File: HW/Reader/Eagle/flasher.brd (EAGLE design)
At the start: 100 x 80 mm, 26 parts, among them Q1 12Mhz, Q1A MMBT3904, Q1B MMBT3904, X1 MINI-USB-SCHIELD-32005-201

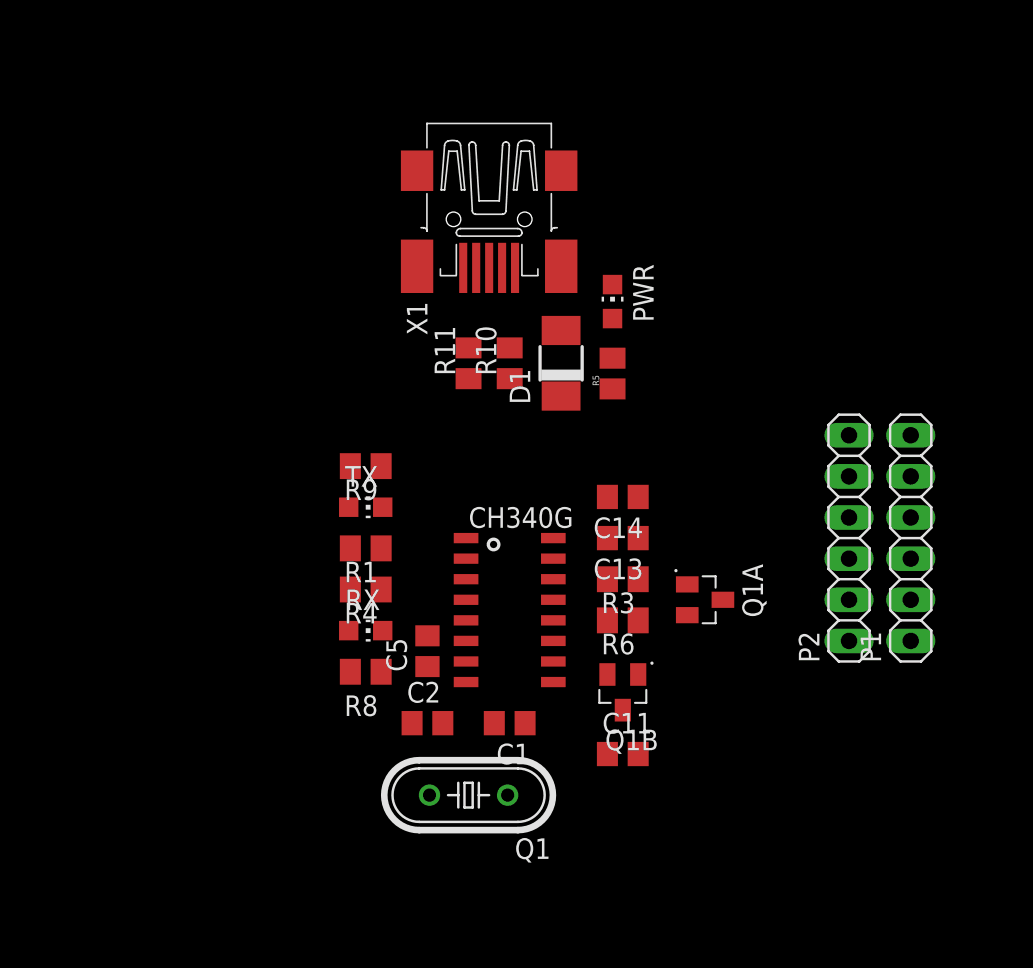
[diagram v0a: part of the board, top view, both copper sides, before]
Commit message: Flasher CH340G SCH & PCB
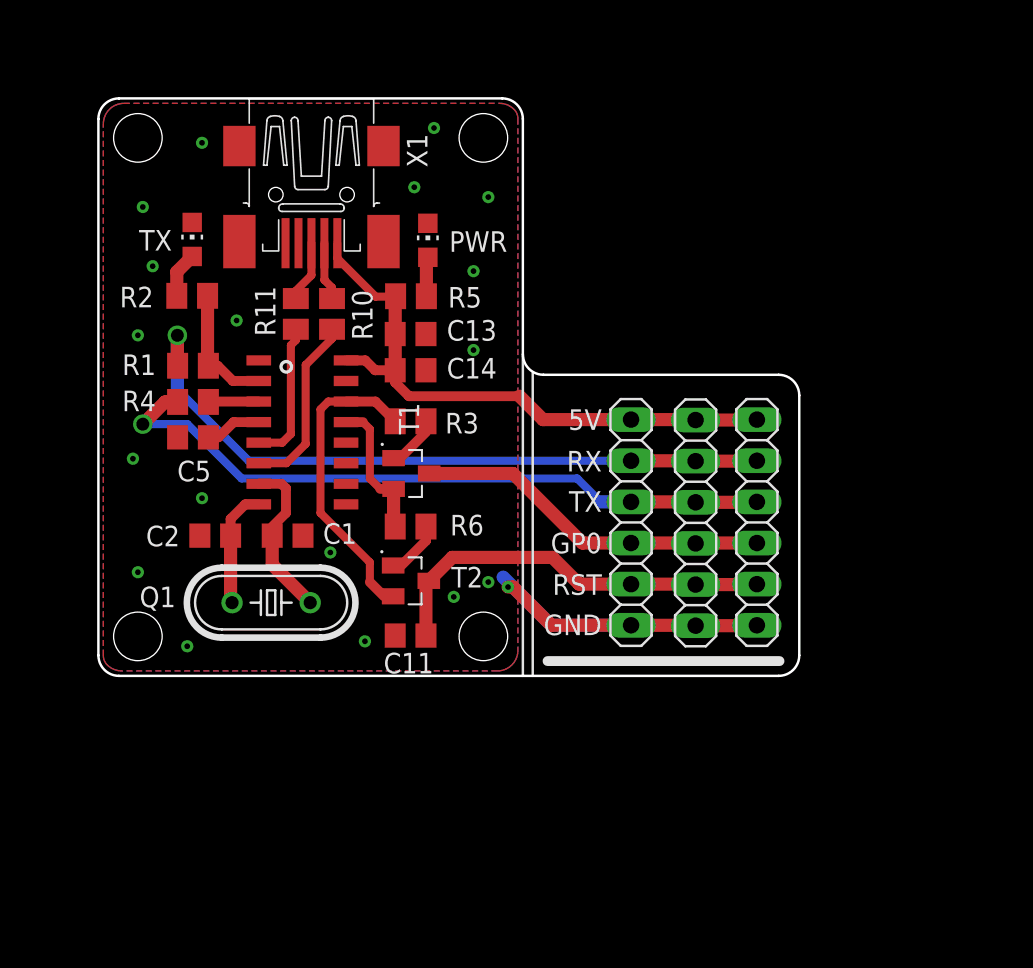
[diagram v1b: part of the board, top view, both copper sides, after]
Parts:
- removed D1: SS14, diode:DO-214AC
- removed Q1A, Q1B: MMBT3904, MMBT3904:SOT95P240X120-3N
- removed R8, R9: 470, rcl:M0805
- removed RX: (no value), led:CHIP-LED0805
- removed U$1: CH340G, ch340g:SOIC16
- added P3: (no value), pinhead:1X06
- added R2: 470, rcl:M0805
- added T1, T2: MMBT3904, MMBT3904:SOT95P240X120-3N
- added U1: CH340G, ch340g:SOIC16
- moved TX 19.7 mm to (36.3, 48.3), turned to 0 degrees
- moved C5 19.6 mm to (36.3, 36.1), turned to 0 degrees
- moved C13 18.2 mm to (49.8, 42.4)
- moved C1 18.0 mm to (42.2, 30.0)
- moved C2 17.5 mm to (37.7, 30.0)
- moved Q1 17.0 mm to (41.1, 25.9)
- moved R3 16.3 mm to (49.8, 37.1)
- moved R4 15.7 mm to (36.3, 38.3)
- moved R1 15.5 mm to (36.3, 40.5)
- moved C14 15.3 mm to (49.8, 40.2)
- moved C11 15.0 mm to (49.8, 23.8)
- moved R6 14.3 mm to (49.8, 30.6)
- moved R5 13.3 mm to (49.8, 44.8), turned to 0 degrees
- moved PWR 12.0 mm to (50.8, 48.2)
- moved R10 11.4 mm to (44.9, 43.7)
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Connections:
- removed net N$7: R9.2, TX.A
- removed net VIN: D1.A, P1.1, P2.1, X1.1
- net +5V: now also P1.1, P2.1, P3.1, U1.16, X1.1; no longer D1.C, R8.1, R9.1, U$1.16
- net D+: now also U1.5; no longer U$1.5
- net D-: now also U1.6; no longer U$1.6
- net DTR: now also T1.2, U1.13; no longer Q1A.2, U$1.13
- net GND: now also P3.6, TX.C, U1.1; no longer U$1.1
- net GPIO0: now also P3.4, T1.3; no longer Q1A.3
- net N$1: now also R2.2, U1.2; no longer TX.C, U$1.2
- net N$12: now also U1.4; no longer U$1.4
- net N$16: now also U1.7; no longer U$1.7
- net N$17: now also U1.8; no longer U$1.8
- net N$2: now also U1.3; no longer RX.C, U$1.3
- net N$4: now also R2.1, TX.A; no longer R8.2, RX.A
- net N$5: now also T1.1; no longer Q1A.1
- net N$6: now also T2.1; no longer Q1B.1
- net RESET: now also P3.5, T2.3; no longer Q1B.3
- net RTS: now also T2.2, U1.14; no longer Q1B.2, U$1.14
- net RXD: now also P3.2
- net TXD: now also P3.3
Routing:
- net RXD: track 0.00 -> 42.9 mm, vias 0 -> 1
- net TXD: track 0.00 -> 42.6 mm, vias 0 -> 1
- net +5V: track 0.00 -> 37.4 mm
- net RESET: track 0.00 -> 25.6 mm
- net GND: track 0.00 -> 25.5 mm, vias 0 -> 19
- net GPIO0: track 0.00 -> 22.0 mm
- net RTS: track 0.00 -> 19.5 mm
- net D-: track 0.00 -> 11.1 mm
- net N$16: track 0.00 -> 10.2 mm
- net DTR: track 0.00 -> 8.80 mm
- net D+: track 0.00 -> 8.80 mm
- net N$1: track 0.00 -> 7.84 mm
- net N$17: track 0.00 -> 7.32 mm
- net N$9: track 0.00 -> 3.82 mm
- net N$8: track 0.00 -> 3.61 mm
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- added copper zone on layer 1, net GND
- added copper zone on layer 16, net GND
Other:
- outline, holes or cut-outs redrawn
- board text added: "5V"
- board text added: "GND"
- board text added: "GP0"
- board text added: "RST"
- board text added: "RX"
- board text added: "TX"

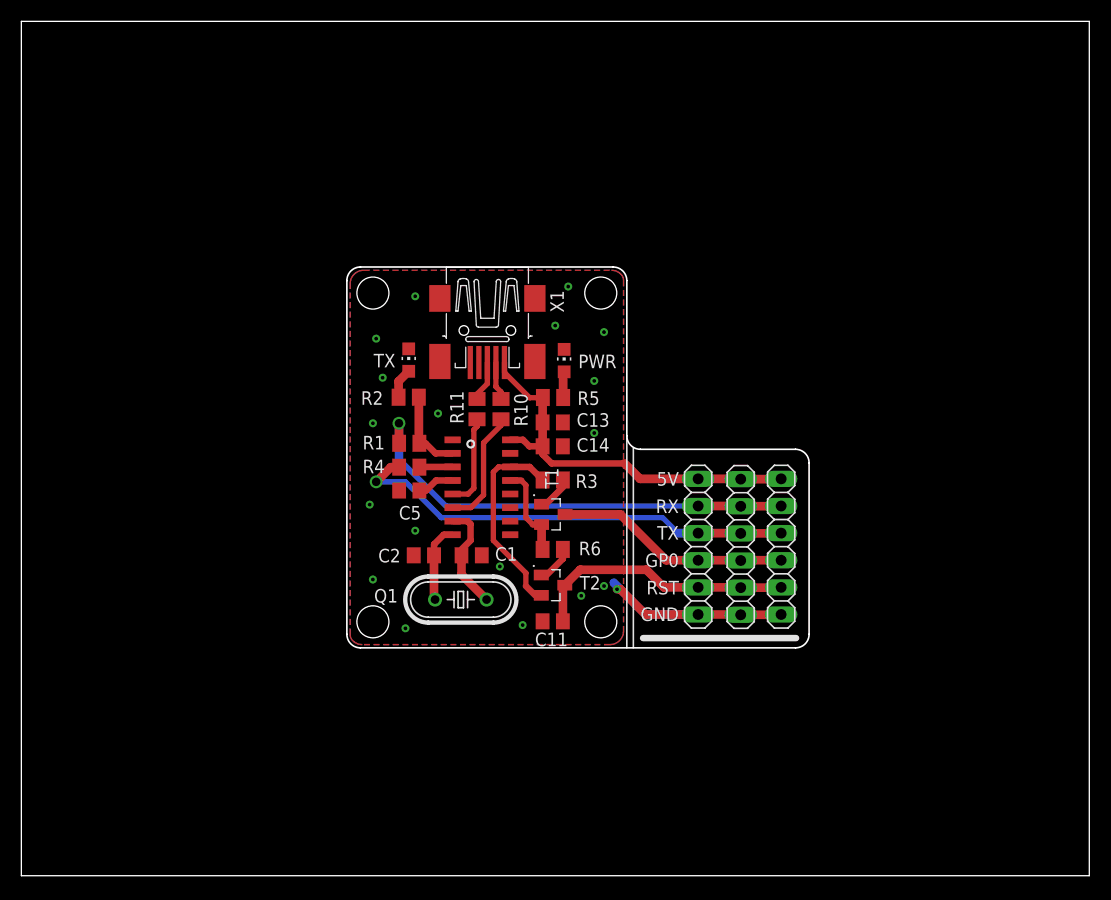
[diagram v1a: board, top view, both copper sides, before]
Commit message: Flasher Update
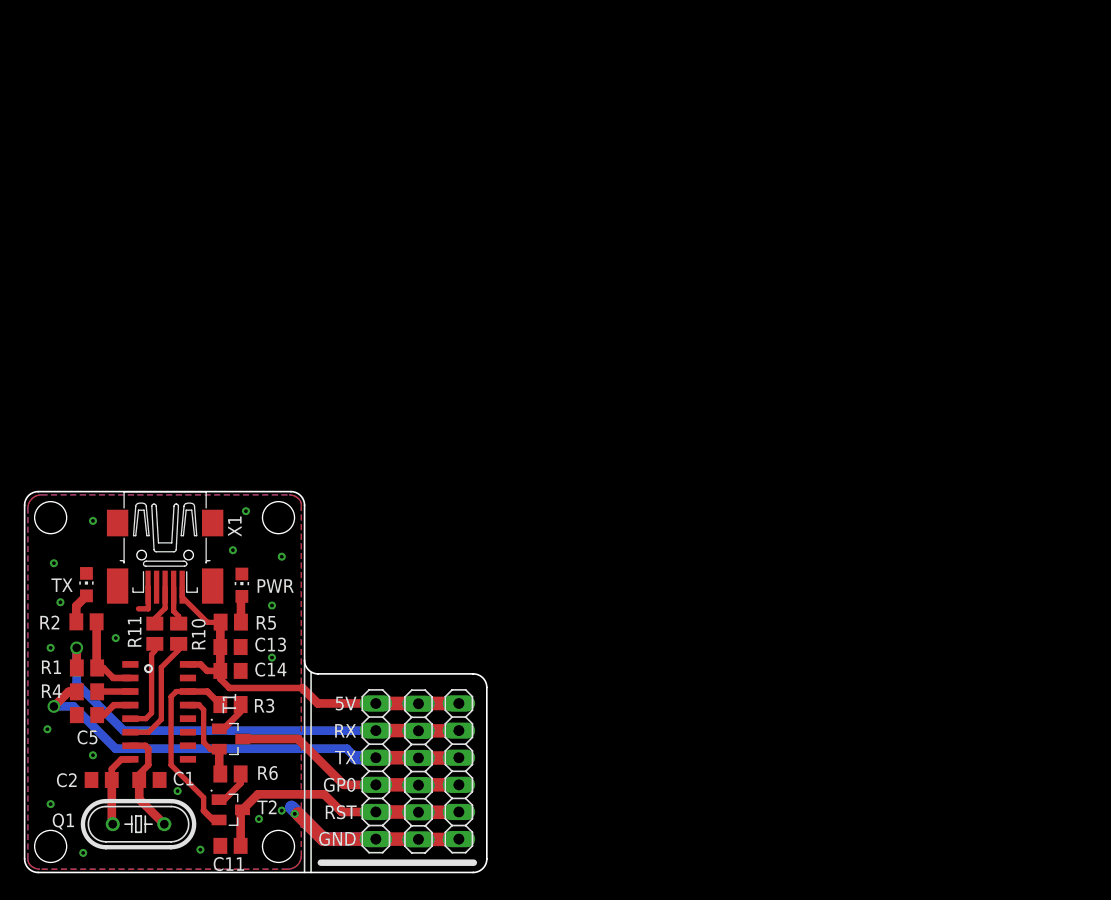
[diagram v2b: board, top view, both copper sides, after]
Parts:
- moved C1 36.8 mm to (12.0, 8.97)
- moved C11 36.8 mm to (19.6, 2.79)
- moved C13 36.8 mm to (19.6, 21.4)
- moved C14 36.8 mm to (19.6, 19.2)
- moved C2 36.8 mm to (7.52, 8.97)
- moved C5 36.8 mm to (6.15, 15.0)
- moved P1 36.8 mm to (41.0, 9.78)
- moved P2 36.8 mm to (37.2, 9.75)
- moved P3 36.8 mm to (33.2, 9.78)
- moved PWR 36.8 mm to (20.7, 27.2)
- moved Q1 36.8 mm to (11.0, 4.83)
- moved R1 36.8 mm to (6.15, 19.5)
- moved R10 36.8 mm to (14.7, 22.7)
- moved R11 36.8 mm to (12.5, 22.7)
- moved R2 36.8 mm to (6.10, 23.8)
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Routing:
- net GND: track 25.5 -> 28.5 mm
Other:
- board size 100 x 80 mm -> 43.3 x 35.7 mm
